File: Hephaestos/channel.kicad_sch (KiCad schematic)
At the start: 11 parts, among them J3 Conn_01x02, U1 MCP6001-OT

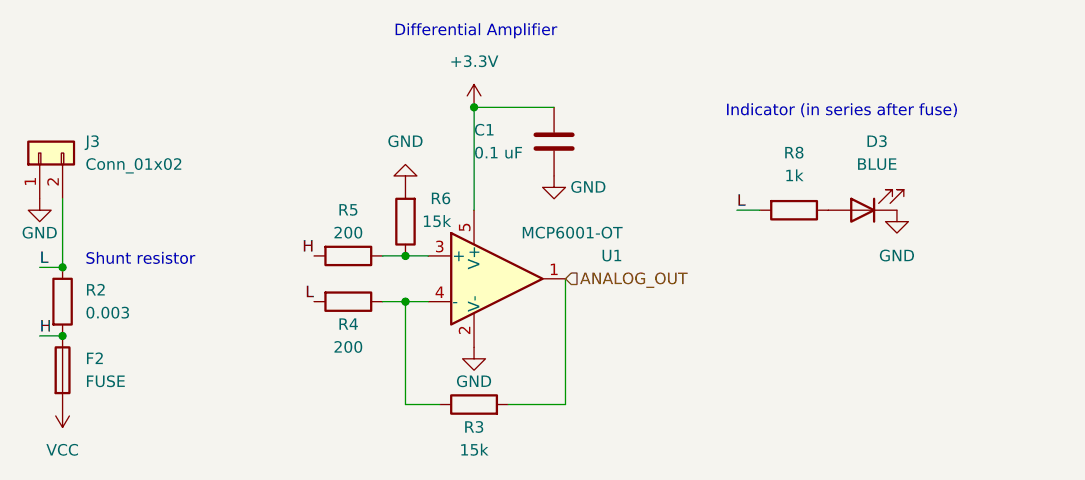
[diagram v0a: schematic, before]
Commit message: Downgrade CAN controller to 2.0B for driver compatibility
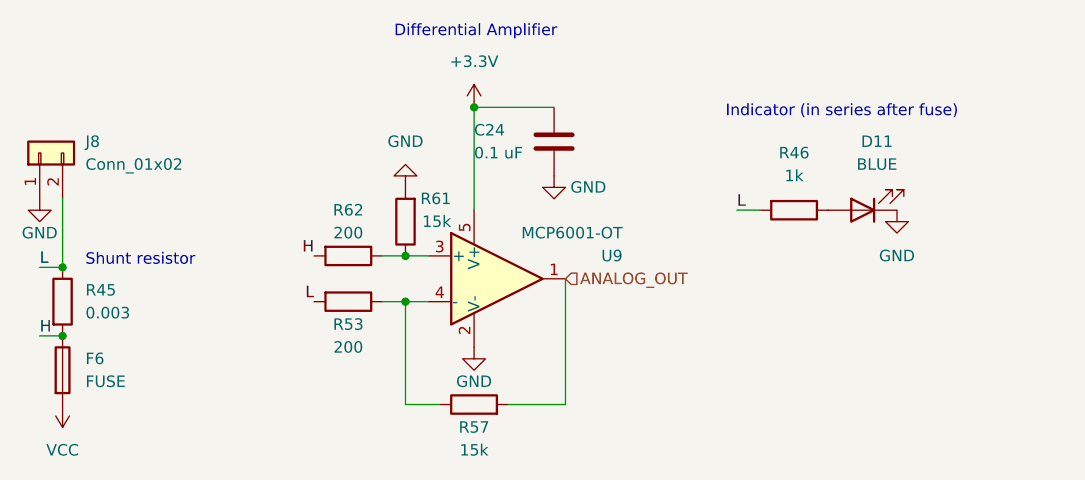
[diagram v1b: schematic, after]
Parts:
- renumbered C1 to C24, D3 to D11, F2 to F6, J3 to J8, R2 to R45, R8 to R46, R4 to R53, R3 to R57, R6 to R61, R5 to R62, U1 to U9

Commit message: Switch to F042 w/ internal CAN controller, change stackup
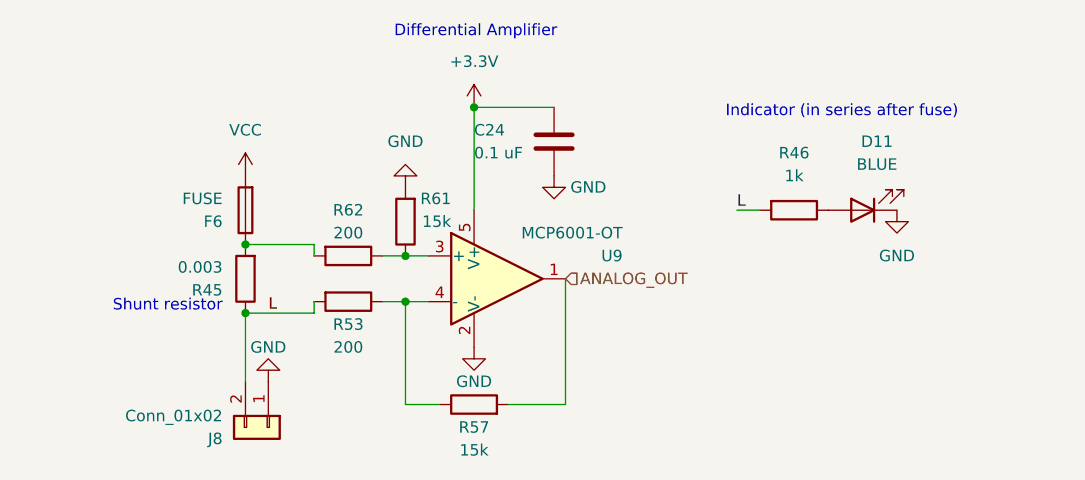
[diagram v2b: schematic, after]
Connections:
- net H: no longer names the net of F6.1, R45.2, R62.2
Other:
- moved on the sheet: F6, J8, R45
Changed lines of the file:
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@@
   (junction (at 91.44 91.44) (diameter 0) (color 0 0 0 0)
   )
+  (junction (at 73.66 85.09) (diameter 0) (color 0 0 0 0)
+  )
   (junction (at 91.44 86.36) (diameter 0) (color 0 0 0 0)
   )
-  (junction (at 53.34 95.25) (diameter 0) (color 0 0 0 0)
-  )
   (junction (at 99.06 69.85) (diameter 0) (color 0 0 0 0)
   )
-  (junction (at 53.34 87.63) (diameter 0) (color 0 0 0 0)
+  (junction (at 73.66 92.71) (diameter 0) (color 0 0 0 0)
   )
   (wire (pts (xy 93.98 91.44) (xy 91.44 91.44))
@@
     (stroke (width 0) (type default))
   )
+  (wire (pts (xy 81.28 91.44) (xy 81.28 92.71))
+    (stroke (width 0) (type default))
+  )
   (wire (pts (xy 128.27 81.28) (xy 130.81 81.28))
     (stroke (width 0) (type default))
   )
+  (wire (pts (xy 81.28 86.36) (xy 81.28 85.09))
+    (stroke (width 0) (type default))
+  )
   (wire (pts (xy 99.06 69.85) (xy 107.95 69.85))
     (stroke (width 0) (type default))
@@
     (stroke (width 0) (type default))
   )
-  (wire (pts (xy 53.34 80.01) (xy 53.34 87.63))
+  (wire (pts (xy 73.66 100.33) (xy 73.66 92.71))
     (stroke (width 0) (type default))
   )
@@
     (stroke (width 0) (type default))
   )
-  (wire (pts (xy 50.8 95.25) (xy 53.34 95.25))
+  (wire (pts (xy 73.66 92.71) (xy 81.28 92.71))
     (stroke (width 0) (type default))
   )
@@
     (stroke (width 0) (type default))
   )
-  (wire (pts (xy 50.8 87.63) (xy 53.34 87.63))
+  (wire (pts (xy 73.66 85.09) (xy 81.28 85.09))
     (stroke (width 0) (type default))
   )
@@
     (effects (font (size 1.27 1.27)) (justify left bottom))
   )
-  (text "Shunt resistor" (at 55.88 87.63 0)
-    (effects (font (size 1.27 1.27)) (justify left bottom))
+  (text "Shunt resistor" (at 71.12 92.71 0)
+    (effects (font (size 1.27 1.27)) (justify right bottom))
   )
   (text "Indicator (in series after fuse)" (at 127 71.12 0)
     (effects (font (size 1.27 1.27)) (justify left bottom))
   )
-  (label "L" (at 81.28 91.44 180) (fields_autoplaced)
-    (effects (font (size 1.27 1.27)) (justify right bottom))
-  )
-  (label "H" (at 81.28 86.36 180) (fields_autoplaced)
-    (effects (font (size 1.27 1.27)) (justify right bottom))
+  (label "L" (at 76.2 92.71 0) (fields_autoplaced)
+    (effects (font (size 1.27 1.27)) (justify left bottom))
   )
   (label "L" (at 128.27 81.28 0) (fields_autoplaced)
     (effects (font (size 1.27 1.27)) (justify left bottom))
   )
-  (label "H" (at 50.8 95.25 0) (fields_autoplaced)
-    (effects (font (size 1.27 1.27)) (justify left bottom))
-  )
-  (label "L" (at 50.8 87.63 0) (fields_autoplaced)
-    (effects (font (size 1.27 1.27)) (justify left bottom))
-  )
   (hierarchical_label "ANALOG_OUT" (shape input) (at 109.22 88.9 0) (fields_autoplaced)
     (effects (font (size 1.27 1.27)) (justify left))
   )
-  (symbol (lib_id "Connector_Generic:Conn_01x02") (at 50.8 74.93 90) (unit 1)
+  (symbol (lib_id "Connector_Generic:Conn_01x02") (at 76.2 105.41 270) (unit 1)
     (in_bom yes) (on_board yes) (dnp no) (fields_autoplaced)
-    (property "Reference" "J8" (at 55.88 73.6599 90)
+    (property "Reference" "J8" (at 71.12 106.6801 90)
       (effects (font (size 1.27 1.27)) (justify right))
     )
-    (property "Value" "Conn_01x02" (at 55.88 76.1999 90)
+    (property "Value" "Conn_01x02" (at 71.12 104.1401 90)
       (effects (font (size 1.27 1.27)) (justify right))
     )
-    (property "Footprint" "Connector_JST:JST_VH_B2P-VH-B_1x02_P3.96mm_Vertical" (at 50.8 74.93 0)
-      (effects (font (size 1.27 1.27)) hide)
-    )
-    (property "Datasheet" "~" (at 50.8 74.93 0)
-      (effects (font (size 1.27 1.27)) hide)
-    )
-    (property "JLCPCB_IGNORE" "~" (at 50.8 74.93 90)
+    (property "Footprint" "Connector_JST:JST_VH_B2P-VH-B_1x02_P3.96mm_Vertical" (at 76.2 105.41 0)
+      (effects (font (size 1.27 1.27)) hide)
+    )
+    (property "Datasheet" "~" (at 76.2 105.41 0)
+      (effects (font (size 1.27 1.27)) hide)
+    )
+    (property "JLCPCB_IGNORE" "~" (at 76.2 105.41 90)
       (effects (font (size 1.27 1.27)) hide)
     )
@@
     )
   )
-  (symbol (lib_id "power:VCC") (at 53.34 102.87 180) (unit 1)
+  (symbol (lib_id "power:VCC") (at 73.66 77.47 0) (unit 1)
     (in_bom yes) (on_board yes) (dnp no) (fields_autoplaced)
-    (property "Reference" "#PWR035" (at 53.34 99.06 0)
-      (effects (font (size 1.27 1.27)) hide)
-    )
-    (property "Value" "VCC" (at 53.34 107.95 0)
-      (effects (font (size 1.27 1.27)))
-    )
-    (property "Footprint" "" (at 53.34 102.87 0)
-      (effects (font (size 1.27 1.27)) hide)
-    )
-    (property "Datasheet" "" (at 53.34 102.87 0)
+    (property "Reference" "#PWR035" (at 73.66 81.28 0)
+      (effects (font (size 1.27 1.27)) hide)
+    )
+    (property "Value" "VCC" (at 73.66 72.39 0)
+      (effects (font (size 1.27 1.27)))
+    )
+    (property "Footprint" "" (at 73.66 77.47 0)
+      (effects (font (size 1.27 1.27)) hide)
+    )
+    (property "Datasheet" "" (at 73.66 77.47 0)
       (effects (font (size 1.27 1.27)) hide)
     )
@@
     )
   )
-  (symbol (lib_id "power:GND") (at 50.8 80.01 0) (unit 1)
-    (in_bom yes) (on_board yes) (dnp no)
-    (property "Reference" "#PWR07" (at 50.8 86.36 0)
-      (effects (font (size 1.27 1.27)) hide)
-    )
-    (property "Value" "GND" (at 50.8 83.82 0)
-      (effects (font (size 1.27 1.27)))
-    )
-    (property "Footprint" "" (at 50.8 80.01 0)
-      (effects (font (size 1.27 1.27)) hide)
-    )
-    (property "Datasheet" "" (at 50.8 80.01 0)
+  (symbol (lib_id "power:GND") (at 76.2 100.33 180) (unit 1)
+    (in_bom yes) (on_board yes) (dnp no)
+    (property "Reference" "#PWR07" (at 76.2 93.98 0)
+      (effects (font (size 1.27 1.27)) hide)
+    )
+    (property "Value" "GND" (at 76.2 96.52 0)
+      (effects (font (size 1.27 1.27)))
+    )
+    (property "Footprint" "" (at 76.2 100.33 0)
+      (effects (font (size 1.27 1.27)) hide)
+    )
+    (property "Datasheet" "" (at 76.2 100.33 0)
       (effects (font (size 1.27 1.27)) hide)
     )
@@
     )
   )
-  (symbol (lib_id "Device:Fuse") (at 53.34 99.06 0) (unit 1)
+  (symbol (lib_id "Device:Fuse") (at 73.66 81.28 180) (unit 1)
     (in_bom yes) (on_board yes) (dnp no) (fields_autoplaced)
-    (property "Reference" "F6" (at 55.88 97.7899 0)
+    (property "Reference" "F6" (at 71.12 82.5501 0)
       (effects (font (size 1.27 1.27)) (justify left))
     )
-    (property "Value" "FUSE" (at 55.88 100.3299 0)
+    (property "Value" "FUSE" (at 71.12 80.0101 0)
       (effects (font (size 1.27 1.27)) (justify left))
     )
-    (property "Footprint" "Fuse:Fuseholder_Blade_Mini_Keystone_3568" (at 51.562 99.06 90)
-      (effects (font (size 1.27 1.27)) hide)
-    )
-    (property "Datasheet" "~" (at 53.34 99.06 0)
-      (effects (font (size 1.27 1.27)) hide)
-    )
-    (property "JLCPCB_IGNORE" "~" (at 53.34 99.06 0)
+    (property "Footprint" "Fuse:Fuseholder_Blade_Mini_Keystone_3568" (at 75.438 81.28 90)
+      (effects (font (size 1.27 1.27)) hide)
+    )
+    (property "Datasheet" "~" (at 73.66 81.28 0)
+      (effects (font (size 1.27 1.27)) hide)
+    )
+    (property "JLCPCB_IGNORE" "~" (at 73.66 81.28 0)
       (effects (font (size 1.27 1.27)) hide)
     )
@@
     )
   )
-  (symbol (lib_id "Device:R") (at 53.34 91.44 0) (unit 1)
-    (in_bom yes) (on_board yes) (dnp no)
-    (property "Reference" "R45" (at 55.88 90.17 0)
+  (symbol (lib_id "Device:R") (at 73.66 88.9 180) (unit 1)
+    (in_bom yes) (on_board yes) (dnp no)
+    (property "Reference" "R45" (at 71.12 90.17 0)
       (effects (font (size 1.27 1.27)) (justify left))
     )
-    (property "Value" "0.003" (at 55.88 92.7099 0)
+    (property "Value" "0.003" (at 71.12 87.6301 0)
       (effects (font (size 1.27 1.27)) (justify left))
     )
-    (property "Footprint" "Resistor_SMD:R_0805_2012Metric" (at 51.562 91.44 90)
-      (effects (font (size 1.27 1.27)) hide)
-    )
-    (property "Datasheet" "~" (at 53.34 91.44 0)
-      (effects (font (size 1.27 1.27)) hide)
-    )
+    (property "Footprint" "Resistor_SMD:R_0805_2012Metric" (at 75.438 88.9 90)
+      (effects (font (size 1.27 1.27)) hide)
+    )
+    (property "Datasheet" "~" (at 73.66 88.9 0)
+      (effects (font (size 1.27 1.27)) hide)
+    )

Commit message: Add second bulk cap
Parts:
- renumbered C24 to C20, R45 to R44, R46 to R45, R53 to R52, R57 to R56, R61 to R60, R62 to R61, U9 to U8
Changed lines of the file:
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@@
   (symbol (lib_id "Device:R") (at 99.06 102.87 90) (unit 1)
     (in_bom yes) (on_board yes) (dnp no)
-    (property "Reference" "R57" (at 99.06 105.41 90)
+    (property "Reference" "R56" (at 99.06 105.41 90)
       (effects (font (size 1.27 1.27)))
     )
@@
       (project "Hephaestos"
         (path "/1d341529-07cc-4307-9d8a-f04b27be88a3/b56cf97a-1d8f-494b-a267-659a81a9e13a"
+          (reference "R56") (unit 1)
+        )
+        (path "/1d341529-07cc-4307-9d8a-f04b27be88a3/4a79c44b-7bf4-4348-bb5e-7f546e809505"
           (reference "R57") (unit 1)
         )
-        (path "/1d341529-07cc-4307-9d8a-f04b27be88a3/4a79c44b-7bf4-4348-bb5e-7f546e809505"
+        (path "/1d341529-07cc-4307-9d8a-f04b27be88a3/2449b257-04af-475b-95bd-57e025d81925"
           (reference "R58") (unit 1)
         )
-        (path "/1d341529-07cc-4307-9d8a-f04b27be88a3/2449b257-04af-475b-95bd-57e025d81925"
-          (reference "R59") (unit 1)
-        )
         (path "/1d341529-07cc-4307-9d8a-f04b27be88a3/7e826004-89de-4756-a1d5-ffb37b42eddc"
           (reference "R53") (unit 1)
@@
   (symbol (lib_id "Amplifier_Operational:MCP6001-OT") (at 101.6 88.9 0) (unit 1)
     (in_bom yes) (on_board yes) (dnp no)
-    (property "Reference" "U9" (at 115.57 86.36 0)
+    (property "Reference" "U8" (at 115.57 86.36 0)
       (effects (font (size 1.27 1.27)) (justify right))
     )
@@
       (project "Hephaestos"
         (path "/1d341529-07cc-4307-9d8a-f04b27be88a3/b56cf97a-1d8f-494b-a267-659a81a9e13a"
+          (reference "U8") (unit 1)
+        )
+        (path "/1d341529-07cc-4307-9d8a-f04b27be88a3/4a79c44b-7bf4-4348-bb5e-7f546e809505"
           (reference "U9") (unit 1)
         )
-        (path "/1d341529-07cc-4307-9d8a-f04b27be88a3/4a79c44b-7bf4-4348-bb5e-7f546e809505"
+        (path "/1d341529-07cc-4307-9d8a-f04b27be88a3/2449b257-04af-475b-95bd-57e025d81925"
           (reference "U10") (unit 1)
         )
-        (path "/1d341529-07cc-4307-9d8a-f04b27be88a3/2449b257-04af-475b-95bd-57e025d81925"
-          (reference "U11") (unit 1)
-        )
         (path "/1d341529-07cc-4307-9d8a-f04b27be88a3/7e826004-89de-4756-a1d5-ffb37b42eddc"
           (reference "U12") (unit 1)
@@
   (symbol (lib_id "Device:C") (at 107.95 73.66 0) (unit 1)
     (in_bom yes) (on_board yes) (dnp no)
-    (property "Reference" "C24" (at 99.06 72.39 0)
+    (property "Reference" "C20" (at 99.06 72.39 0)
       (effects (font (size 1.27 1.27)) (justify left))
     )
@@
       (project "Hephaestos"
         (path "/1d341529-07cc-4307-9d8a-f04b27be88a3/b56cf97a-1d8f-494b-a267-659a81a9e13a"
-          (reference "C24") (unit 1)
-        )
-        (path "/1d341529-07cc-4307-9d8a-f04b27be88a3/4a79c44b-7bf4-4348-bb5e-7f546e809505"
-          (reference "C25") (unit 1)
-        )
-        (path "/1d341529-07cc-4307-9d8a-f04b27be88a3/2449b257-04af-475b-95bd-57e025d81925"
-          (reference "C26") (unit 1)
+          (reference "C20") (unit 1)
+        )
+        (path "/1d341529-07cc-4307-9d8a-f04b27be88a3/4a79c44b-7bf4-4348-bb5e-7f546e809505"
+          (reference "C21") (unit 1)
+        )
+        (path "/1d341529-07cc-4307-9d8a-f04b27be88a3/2449b257-04af-475b-95bd-57e025d81925"
+          (reference "C22") (unit 1)
         )
         (path "/1d341529-07cc-4307-9d8a-f04b27be88a3/7e826004-89de-4756-a1d5-ffb37b42eddc"
@@
   (symbol (lib_id "Device:R") (at 85.09 86.36 270) (unit 1)
     (in_bom yes) (on_board yes) (dnp no)
-    (property "Reference" "R62" (at 85.09 81.28 90)
+    (property "Reference" "R61" (at 85.09 81.28 90)
       (effects (font (size 1.27 1.27)))
     )
@@
       (project "Hephaestos"
         (path "/1d341529-07cc-4307-9d8a-f04b27be88a3/b56cf97a-1d8f-494b-a267-659a81a9e13a"
-          (reference "R62") (unit 1)
-        )
-        (path "/1d341529-07cc-4307-9d8a-f04b27be88a3/4a79c44b-7bf4-4348-bb5e-7f546e809505"
-          (reference "R64") (unit 1)
-        )
-        (path "/1d341529-07cc-4307-9d8a-f04b27be88a3/2449b257-04af-475b-95bd-57e025d81925"
-          (reference "R66") (unit 1)
+          (reference "R61") (unit 1)
+        )
+        (path "/1d341529-07cc-4307-9d8a-f04b27be88a3/4a79c44b-7bf4-4348-bb5e-7f546e809505"
+          (reference "R63") (unit 1)
+        )
+        (path "/1d341529-07cc-4307-9d8a-f04b27be88a3/2449b257-04af-475b-95bd-57e025d81925"
+          (reference "R65") (unit 1)
         )
         (path "/1d341529-07cc-4307-9d8a-f04b27be88a3/7e826004-89de-4756-a1d5-ffb37b42eddc"
@@
   (symbol (lib_id "Device:R") (at 91.44 82.55 180) (unit 1)
     (in_bom yes) (on_board yes) (dnp no)
-    (property "Reference" "R61" (at 96.52 80.01 0)
+    (property "Reference" "R60" (at 96.52 80.01 0)
       (effects (font (size 1.27 1.27)) (justify left))
     )
@@
       (project "Hephaestos"
         (path "/1d341529-07cc-4307-9d8a-f04b27be88a3/b56cf97a-1d8f-494b-a267-659a81a9e13a"
-          (reference "R61") (unit 1)
-        )
-        (path "/1d341529-07cc-4307-9d8a-f04b27be88a3/4a79c44b-7bf4-4348-bb5e-7f546e809505"
-          (reference "R63") (unit 1)
-        )
-        (path "/1d341529-07cc-4307-9d8a-f04b27be88a3/2449b257-04af-475b-95bd-57e025d81925"
-          (reference "R65") (unit 1)
+          (reference "R60") (unit 1)
+        )
+        (path "/1d341529-07cc-4307-9d8a-f04b27be88a3/4a79c44b-7bf4-4348-bb5e-7f546e809505"
+          (reference "R62") (unit 1)
+        )
+        (path "/1d341529-07cc-4307-9d8a-f04b27be88a3/2449b257-04af-475b-95bd-57e025d81925"
+          (reference "R64") (unit 1)
         )
         (path "/1d341529-07cc-4307-9d8a-f04b27be88a3/7e826004-89de-4756-a1d5-ffb37b42eddc"
@@
   (symbol (lib_id "Device:R") (at 73.66 88.9 180) (unit 1)
     (in_bom yes) (on_board yes) (dnp no)
-    (property "Reference" "R45" (at 71.12 90.17 0)
+    (property "Reference" "R44" (at 71.12 90.17 0)
       (effects (font (size 1.27 1.27)) (justify left))
     )
@@
       (project "Hephaestos"
         (path "/1d341529-07cc-4307-9d8a-f04b27be88a3/b56cf97a-1d8f-494b-a267-659a81a9e13a"
-          (reference "R45") (unit 1)
-        )
-        (path "/1d341529-07cc-4307-9d8a-f04b27be88a3/4a79c44b-7bf4-4348-bb5e-7f546e809505"
-          (reference "R47") (unit 1)
-        )
-        (path "/1d341529-07cc-4307-9d8a-f04b27be88a3/2449b257-04af-475b-95bd-57e025d81925"
-          (reference "R49") (unit 1)
+          (reference "R44") (unit 1)
+        )
+        (path "/1d341529-07cc-4307-9d8a-f04b27be88a3/4a79c44b-7bf4-4348-bb5e-7f546e809505"
+          (reference "R46") (unit 1)
+        )
+        (path "/1d341529-07cc-4307-9d8a-f04b27be88a3/2449b257-04af-475b-95bd-57e025d81925"
+          (reference "R48") (unit 1)
         )
         (path "/1d341529-07cc-4307-9d8a-f04b27be88a3/7e826004-89de-4756-a1d5-ffb37b42eddc"
@@
   (symbol (lib_id "Device:R") (at 134.62 81.28 270) (unit 1)
     (in_bom yes) (on_board yes) (dnp no) (fields_autoplaced)
-    (property "Reference" "R46" (at 134.62 74.93 90)
+    (property "Reference" "R45" (at 134.62 74.93 90)
       (effects (font (size 1.27 1.27)))
     )
@@
       (project "Hephaestos"
         (path "/1d341529-07cc-4307-9d8a-f04b27be88a3/b56cf97a-1d8f-494b-a267-659a81a9e13a"
-          (reference "R46") (unit 1)
-        )
-        (path "/1d341529-07cc-4307-9d8a-f04b27be88a3/4a79c44b-7bf4-4348-bb5e-7f546e809505"
-          (reference "R48") (unit 1)
-        )
-        (path "/1d341529-07cc-4307-9d8a-f04b27be88a3/2449b257-04af-475b-95bd-57e025d81925"
-          (reference "R50") (unit 1)
+          (reference "R45") (unit 1)
+        )
+        (path "/1d341529-07cc-4307-9d8a-f04b27be88a3/4a79c44b-7bf4-4348-bb5e-7f546e809505"
+          (reference "R47") (unit 1)
+        )
+        (path "/1d341529-07cc-4307-9d8a-f04b27be88a3/2449b257-04af-475b-95bd-57e025d81925"
+          (reference "R49") (unit 1)
         )
         (path "/1d341529-07cc-4307-9d8a-f04b27be88a3/7e826004-89de-4756-a1d5-ffb37b42eddc"
@@
   (symbol (lib_id "Device:R") (at 85.09 91.44 270) (unit 1)
     (in_bom yes) (on_board yes) (dnp no)
-    (property "Reference" "R53" (at 85.09 93.98 90)
+    (property "Reference" "R52" (at 85.09 93.98 90)
       (effects (font (size 1.27 1.27)))
     )
@@
       (project "Hephaestos"
         (path "/1d341529-07cc-4307-9d8a-f04b27be88a3/b56cf97a-1d8f-494b-a267-659a81a9e13a"
+          (reference "R52") (unit 1)
+        )
+        (path "/1d341529-07cc-4307-9d8a-f04b27be88a3/4a79c44b-7bf4-4348-bb5e-7f546e809505"
           (reference "R53") (unit 1)
         )
-        (path "/1d341529-07cc-4307-9d8a-f04b27be88a3/4a79c44b-7bf4-4348-bb5e-7f546e809505"
+        (path "/1d341529-07cc-4307-9d8a-f04b27be88a3/2449b257-04af-475b-95bd-57e025d81925"
           (reference "R54") (unit 1)
         )
-        (path "/1d341529-07cc-4307-9d8a-f04b27be88a3/2449b257-04af-475b-95bd-57e025d81925"
-          (reference "R55") (unit 1)
-        )
-        (path "/1d341529-07cc-4307-9d8a-f04b27be88a3/7e826004-89de-4756-a1d5-ffb37b42eddc"
+        (path "/1d341529-07cc-4307-9d8a-f04b27be88a3/7e826004-89de-4756-a1d5-ffb37b42eddc"
